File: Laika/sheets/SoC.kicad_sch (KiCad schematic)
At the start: 2 parts, among them J6 Conn_01x03, U1 Milk-V Duo Module

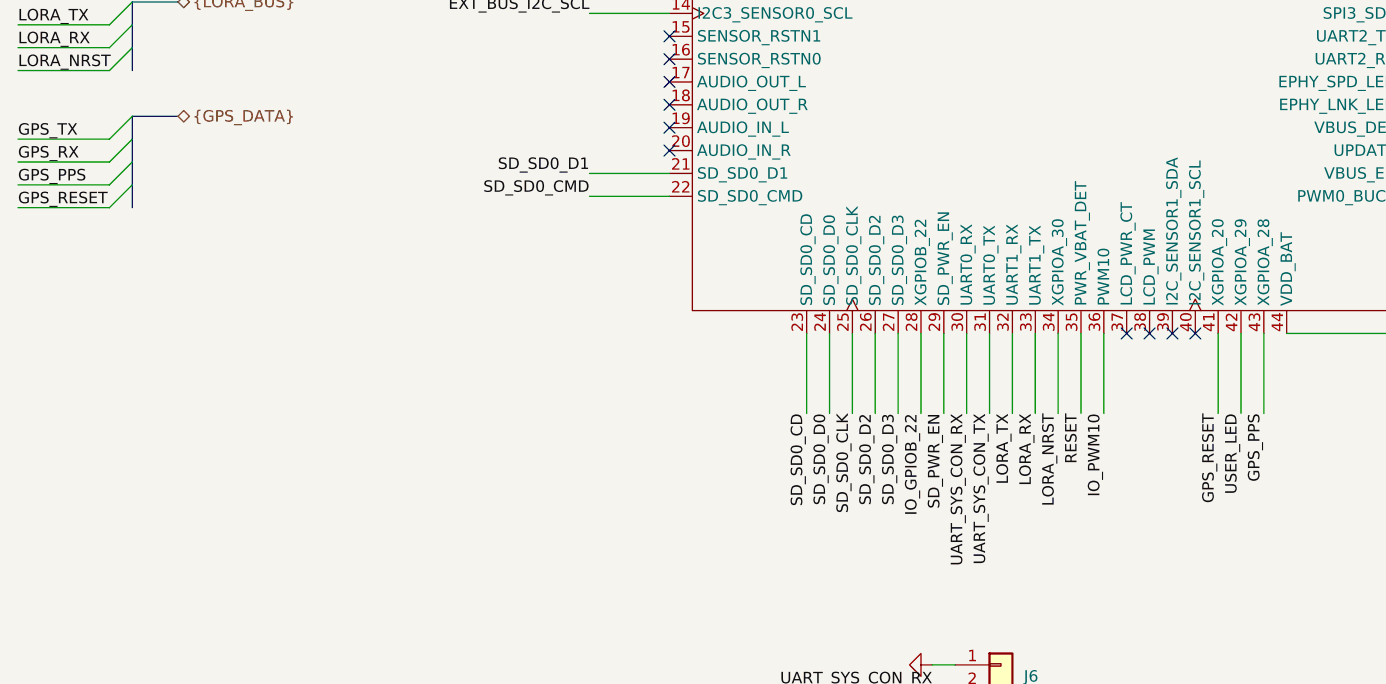
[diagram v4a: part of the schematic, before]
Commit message: Remove external GPS module for spacing constraints
Removed the Ublox GPS module and instead have just a breakout pin
header. While the module technically fit, the amount of free space
around it to follow proper design guidelines left alot of unused space.
To priotize density, GPS design guideslines, and board size, the GPS
will be external.

Signed-off-by: Aeybel Varghese <aeybelvarghese@gmail.com>
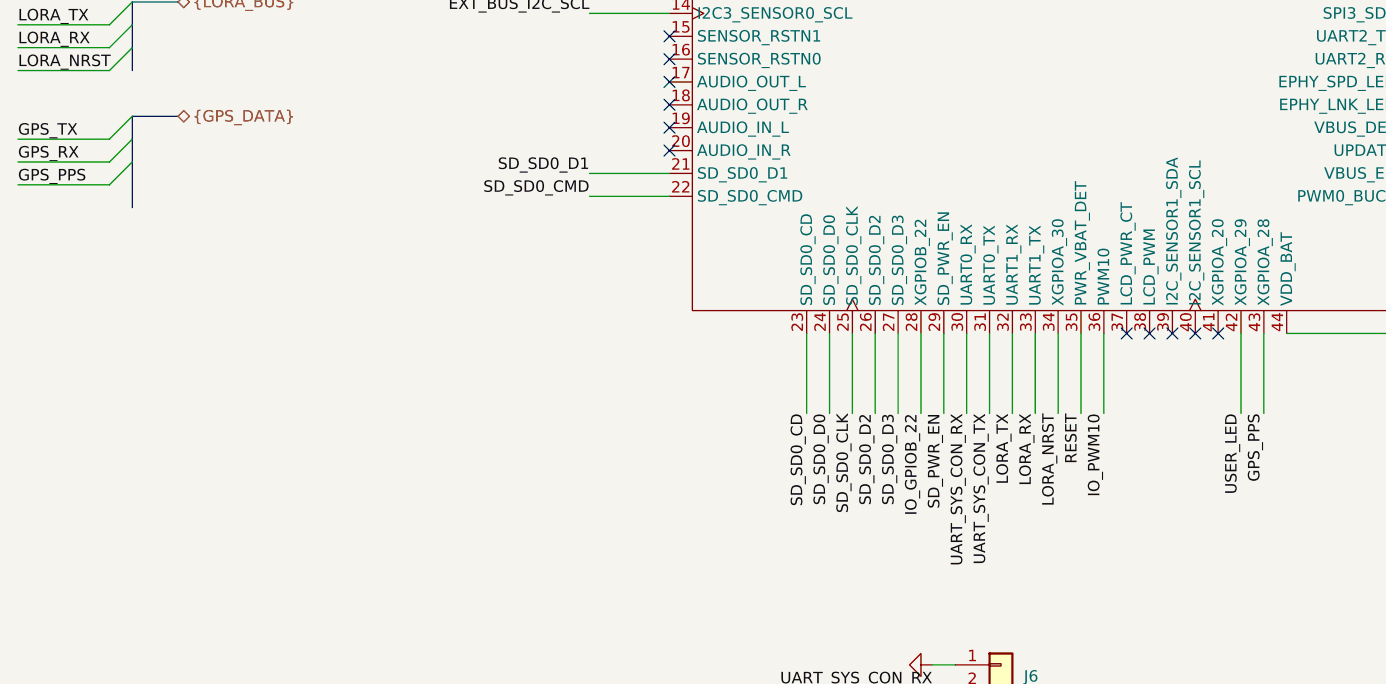
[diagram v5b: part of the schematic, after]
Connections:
- net GPS_RESET: no longer names the net of U1.41 (XGPIOA_20)
- no-connect marks 45 -> 46
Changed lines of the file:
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@@
+	)
+	(no_connect
+		(at 158.75 143.51)
 	)
 	(no_connect
@@
 	)
 	(bus_entry
-		(at 38.1 127)
-		(size -2.54 2.54)
-		(stroke
-			(width 0)
-			(type default)
-		)
-	)
-	(bus_entry
 		(at 38.1 88.9)
 		(size -2.54 2.54)
@@
 		)
 	)
-	(bus
-		(pts
-			(xy 38.1 127) (xy 38.1 129.54)
-		)
-		(stroke
-			(width 0)
-			(type default)
-		)
-	)
 	(wire
 		(pts
@@
 	(wire
 		(pts
-			(xy 25.4 129.54) (xy 35.56 129.54)
-		)
-		(stroke
-			(width 0)
-			(type default)
-		)
-	)
-	(wire
-		(pts
 			(xy 88.9 125.73) (xy 97.79 125.73)
 		)
@@
 		)
 	)
-	(bus
-		(pts
-			(xy 38.1 124.46) (xy 38.1 127)
-		)
-		(stroke
-			(width 0)
-			(type default)
-		)
-	)
 	(wire
 		(pts
@@
 		)
 	)
-	(wire
-		(pts
-			(xy 158.75 152.4) (xy 158.75 143.51)
+	(bus
+		(pts
+			(xy 38.1 124.46) (xy 38.1 129.54)
 		)
 		(stroke
@@
 		)
 	)
-	(label "GPS_RESET"
-		(at 25.4 129.54 0)
-		(effects
-			(font
-				(size 1.27 1.27)
-			)
-			(justify left bottom)
-		)
-	)
 	(label "GPS_PPS"
 		(at 25.4 127 0)
@@
 		)
 	)
-	(label "GPS_RESET"
-		(at 158.75 152.4 270)
-		(effects
-			(font
-				(size 1.27 1.27)
-			)
-			(justify right bottom)
-		)
-	)
